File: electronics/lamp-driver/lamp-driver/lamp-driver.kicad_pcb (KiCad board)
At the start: 2 copper layers, 63.9 x 35.4 mm, 30 parts, among them J1 Conn_01x04_Pin, J12V1 Conn_01x02_Pin, J2 Conn_01x04_Pin, J3 Conn_01x04_Pin, J4 Conn_01x04_Pin, J5 Conn_01x04_Pin, J6 Conn_01x04_Pin, Q1 AO3400A, U1 LM78M05_TO252

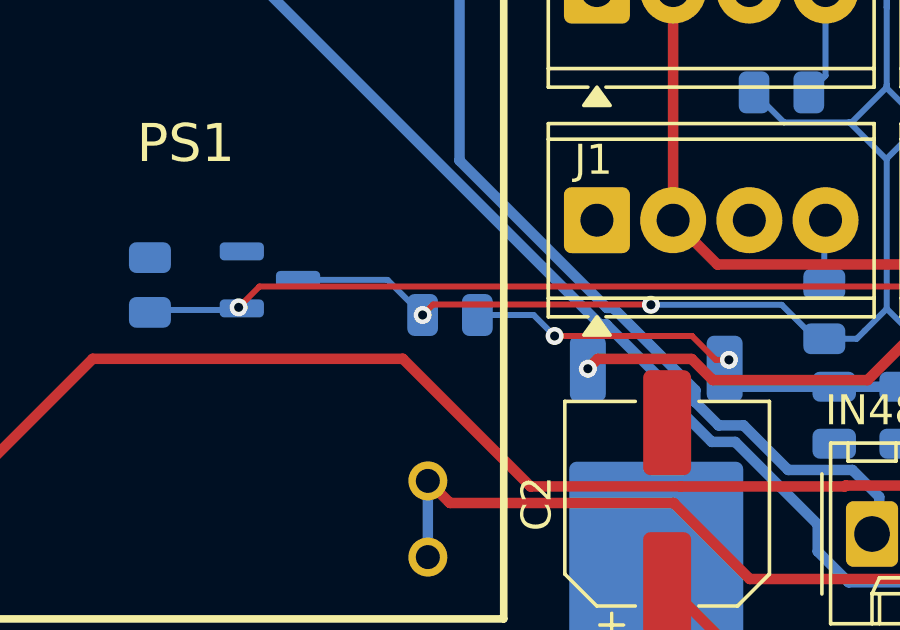
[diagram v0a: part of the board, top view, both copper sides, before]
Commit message: lamp fans control added; uv boost anims added; ambiente light timeout fixed
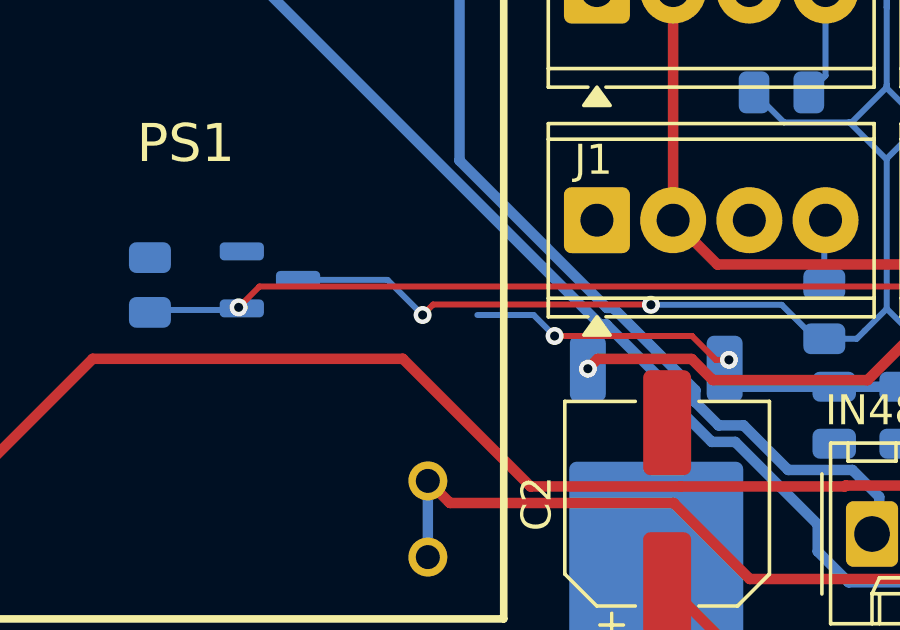
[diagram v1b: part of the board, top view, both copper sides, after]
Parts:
- removed R3: 10K, Resistor_SMD:R_0805_2012Metric
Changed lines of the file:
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@@
 		(tenting front back)
 		(pcbplotparams
-			(layerselection 0x00000000_00000000_55555555_5755f5ff)
+			(layerselection 0x00000000_00000000_55555555_5555d550)
 			(plot_on_all_layers_selection 0x00000000_00000000_00000000_00000000)
 			(disableapertmacros no)
@@
 			(crossoutdnponfab yes)
 			(subtractmaskfromsilk no)
-			(outputformat 1)
+			(outputformat 5)
 			(mirror no)
 			(drillshape 0)
@@
 		)
 		(property "Value" "LM78M05_TO252"
-			(at 0 -4.5 90)
+			(at 12.87 -1.4025 180)
 			(layer "B.Fab")
 			(effects
@@
 			(pintype "passive")
 		)
-		(embedded_fonts no)
-		(model "${KICAD9_3DMODEL_DIR}/Resistor_SMD.3dshapes/R_0805_2012Metric.step"
-			(offset
-				(xyz 0 0 0)
-			)
-			(scale
-				(xyz 1 1 1)
-			)
-			(rotate
-				(xyz 0 0 0)
-			)
-		)
-	)
-	(footprint "Resistor_SMD:R_0805_2012Metric"
-		(layer "B.Cu")
-		(at 112.9425 62.84)
-		(descr "Resistor SMD 0805 (2012 Metric), square (rectangular) end terminal, IPC-7351 nominal, (Body size source: IPC-SM-782 page 72, https://www.pcb-3d.com/wordpress/wp-content/uploads/ipc-sm-782a_amendment_1_and_2.pdf), generated with kicad-footprint-generator")
-		(tags "resistor")
-		(property "Reference" "R3"
-			(at 0 1.65 0)
-			(layer "B.SilkS")
-			(effects
-				(font
-					(size 1 1)
-					(thickness 0.15)
-				)
-				(justify mirror)
-			)
-		)
-		(property "Value" "10K"
-			(at 0 -1.65 0)
-			(layer "B.Fab")
-			(effects
-				(font
-					(size 1 1)
-					(thickness 0.15)
-				)
-				(justify mirror)
-			)
-		)
-		(property "Datasheet" "~"
-			(at 0 0 0)
-			(layer "B.Fab")
-			(hide yes)
-			(effects
-				(font
-					(size 1.27 1.27)
-					(thickness 0.15)
-				)
-				(justify mirror)
-			)
-		)
-		(property "Description" "Resistor, small symbol"
-			(at 0 0 0)
-			(layer "B.Fab")
-			(hide yes)
-			(effects
-				(font
-					(size 1.27 1.27)
-					(thickness 0.15)
-				)
-				(justify mirror)
-			)
-		)
-		(property ki_fp_filters "R_*")
-		(sheetname "/")
-		(sheetfile "lamp-driver.kicad_sch")
-		(attr smd)
-		(fp_line
-			(start -0.227064 -0.735)
-			(end 0.227064 -0.735)
-			(stroke
-				(width 0.12)
-				(type solid)
-			)
-			(layer "B.SilkS")
-		)
-		(fp_line
-			(start -0.227064 0.735)
-			(end 0.227064 0.735)
-			(stroke
-				(width 0.12)
-				(type solid)
-			)
-			(layer "B.SilkS")
-		)
-		(fp_line
-			(start -1.68 -0.95)
-			(end -1.68 0.95)
-			(stroke
-				(width 0.05)
-				(type solid)
-			)
-			(layer "B.CrtYd")
-		)
-		(fp_line
-			(start -1.68 0.95)
-			(end 1.68 0.95)
-			(stroke
-				(width 0.05)
-				(type solid)
-			)
-			(layer "B.CrtYd")
-		)
-		(fp_line
-			(start 1.68 -0.95)
-			(end -1.68 -0.95)
-			(stroke
-				(width 0.05)
-				(type solid)
-			)
-			(layer "B.CrtYd")
-		)
-		(fp_line
-			(start 1.68 0.95)
-			(end 1.68 -0.95)
-			(stroke
-				(width 0.05)
-				(type solid)
-			)
-			(layer "B.CrtYd")
-		)
-		(fp_line
-			(start -1 -0.625)
-			(end -1 0.625)
-			(stroke
-				(width 0.1)
-				(type solid)
-			)
-			(layer "B.Fab")
-		)
-		(fp_line
-			(start -1 0.625)
-			(end 1 0.625)
-			(stroke
-				(width 0.1)
-				(type solid)
-			)
-			(layer "B.Fab")
-		)
-		(fp_line
-			(start 1 -0.625)
-			(end -1 -0.625)
-			(stroke
-				(width 0.1)
-				(type solid)
-			)
-			(layer "B.Fab")
-		)
-		(fp_line
-			(start 1 0.625)
-			(end 1 -0.625)
-			(stroke
-				(width 0.1)
-				(type solid)
-			)
-			(layer "B.Fab")
-		)
-		(fp_text user "${REFERENCE}"
-			(at 0 0 0)
-			(layer "B.Fab")
-			(effects
-				(font
-					(size 0.5 0.5)
-					(thickness 0.08)
-				)
-				(justify mirror)
-			)
-		)
-		(pad "1" smd roundrect
-			(at -0.9125 0)
-			(size 1.025 1.4)
-			(layers "B.Cu" "B.Mask" "B.Paste")
-			(roundrect_rratio 0.243902)
-			(net 10 "pwm_fan")
-			(pintype "passive")
-		)
-		(pad "2" smd roundrect
-			(at 0.9125 0)
-			(size 1.025 1.4)
-			(layers "B.Cu" "B.Mask" "B.Paste")
-			(roundrect_rratio 0.243902)
-			(net 3 "Net-(U1-VO)")
-			(pintype "passive")
-		)

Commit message: uv control fixed
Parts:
- removed R2, R4, R6, R7, R8, R9: 33R, Resistor_SMD:R_0805_2012Metric
- added D2: D_Schottky_SS14, Diode_SMD:D_SMA, B.Cu at (110.9, 58.2)
- added D3: D_Schottky_SS14, Diode_SMD:D_SMA, B.Cu at (110.9, 51.0)
- added D8: D_Schottky_SS14, Diode_SMD:D_SMA, B.Cu at (110.9, 54.6)
- added R3: 10k, Resistor_SMD:R_0805_2012Metric, B.Cu at (108.0, 45.6)
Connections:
- IN48V_1 pad 2: Net-(IN48V_1-Pin_2) -> GND
- J1 pad 1: GND -> pwm_fan
- J1 pad 4: Net-(J1-Pin_4) -> unconnected-(J1-Pin_4-Pad4)
- J2 pad 1: GND -> pwm_fan
- J2 pad 4: Net-(J2-Pin_4) -> unconnected-(J2-Pin_4-Pad4)
- J3 pad 1: GND -> pwm_fan
- J3 pad 4: Net-(J3-Pin_4) -> unconnected-(J3-Pin_4-Pad4)
- J4 pad 1: GND -> pwm_fan
- J4 pad 4: Net-(J4-Pin_4) -> unconnected-(J4-Pin_4-Pad4)
- J5 pad 1: GND -> pwm_fan
- J5 pad 4: Net-(J5-Pin_4) -> unconnected-(J5-Pin_4-Pad4)
- J6 pad 1: GND -> pwm_fan
- J6 pad 4: Net-(J6-Pin_4) -> unconnected-(J6-Pin_4-Pad4)
- PS1 pad 1: Net-(IN48V_1-Pin_2) -> GND
- PS1 pad 2: Net-(IN48V_1-Pin_2) -> GND
- R5 pad 2: GND -> unconnected-(R5-Pad2)
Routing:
- net +12V: track 124.1 -> 180.8 mm, vias 4 -> 5
- net Net-(IN48V_1-Pin_2): track 47.6 -> 0.00 mm
- net pwm_fan: track 73.3 -> 101.7 mm
- net Net-(IN48V_1-Pin_1): track 34.9 -> 53.8 mm
- net Net-(PS1-PWM_DIM): track 72.3 -> 77.8 mm
- net Net-(J2-Pin_4): track 3.63 -> 0.00 mm
- net Net-(J3-Pin_4): track 3.47 -> 0.00 mm
- net Net-(J6-Pin_4): track 3.41 -> 0.00 mm
- net Net-(J5-Pin_4): track 3.41 -> 0.00 mm
- net Net-(J4-Pin_4): track 3.25 -> 0.00 mm
- net GND: track 2.20 -> 4.74 mm, vias 1 -> 3
- net Net-(J1-Pin_4): track 2.14 -> 0.00 mm
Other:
- board text added: "+ -"
